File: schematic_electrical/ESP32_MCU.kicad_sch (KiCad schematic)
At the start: 14 parts, among them U1 ESP32_S2_PICO

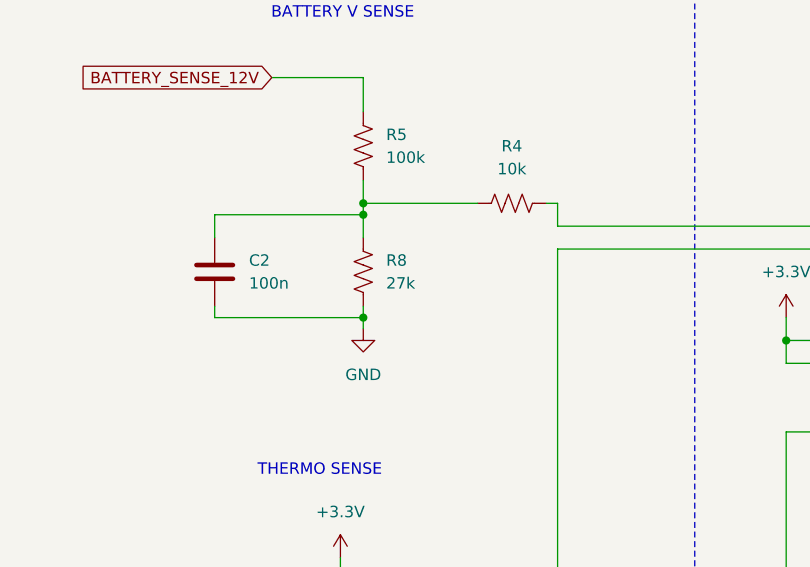
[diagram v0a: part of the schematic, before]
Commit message: Recalibrate thermistor, add reset reason to web UI, increase LED brightness
- Thermistor 2-point calibration redone with equilibrated reference points
  (48.3°F and 116°F); prior calibration used a non-equilibrated 156.9°F point
  that produced a bad slope. New: scale=0.9116, offset=+13.92°F
- Add last_reset_reason to telemetry API and web UI (esp_reset_reason())
- Increase PWM LED brightness from 33% to 66% duty cycle
- Schematic: update R8 value label to 22k (as built), clean CONNECTORS page

Co-Authored-By: Claude Sonnet 4.6 <noreply@anthropic.com>
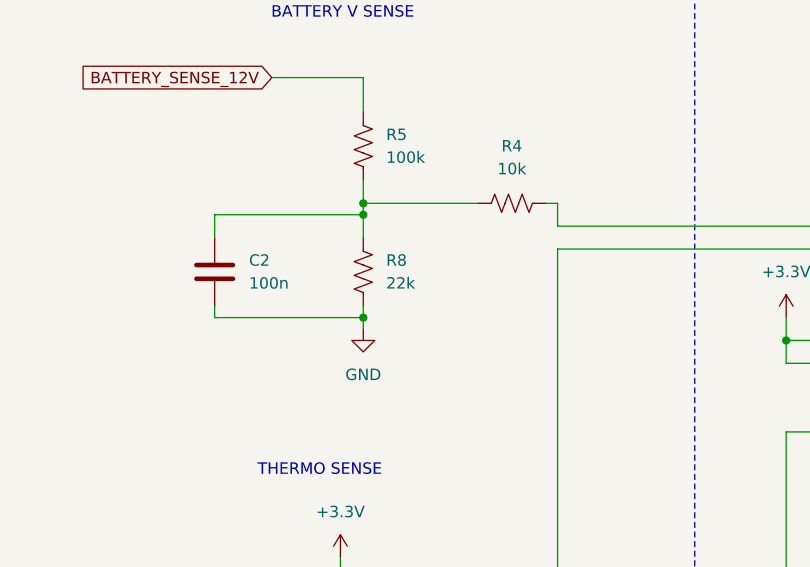
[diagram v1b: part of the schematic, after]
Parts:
- R8: value 27k -> 22k
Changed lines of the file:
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@@
 			)
 		)
-		(property "Value" "27k"
+		(property "Value" "22k"
 			(at 85.09 72.3899 0)
 			(effects

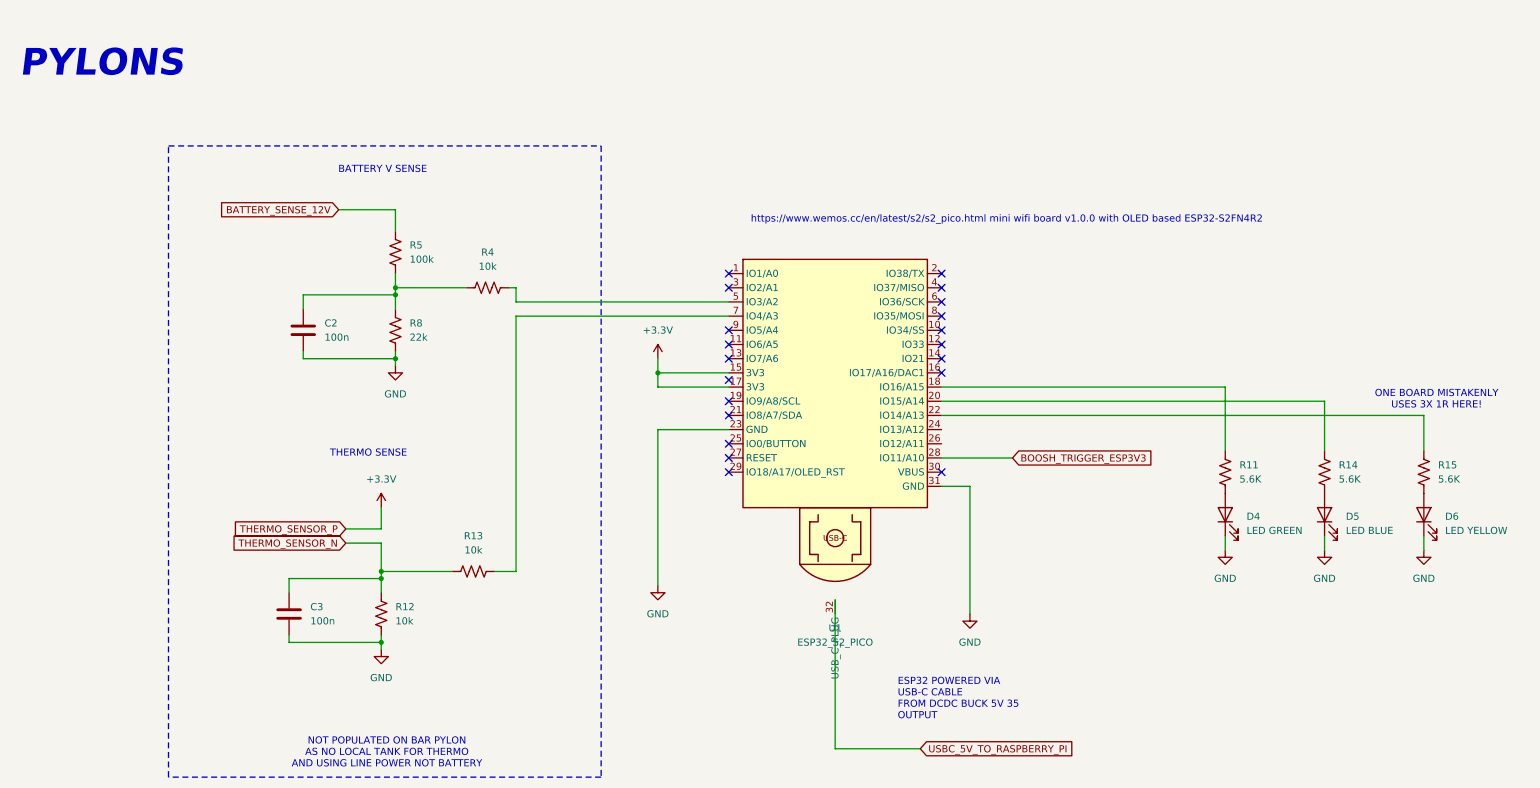
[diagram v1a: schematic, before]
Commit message: Add expansion buttons/lamps schematic sheet; schematic cleanup and annotations
- New EXPANSION_BUTTONS_LAMPS.kicad_sch sheet wired into top-level schematic
- Add AB_800T-QT24 symbol library
- ESP32_MCU: wire previously unconnected GPIO pins to BUTTON0-4 and BUTTON_LAMP_PWM_OUT0-4 global labels; add expansion IO bounding box annotation
- POWER: add GND ganging fabrication notes, DCDC USB wiring note, fuse value updated to "10A MINI AUTO BLADE"; routing cleanup
- CONNECTORS: routing and junction cleanup
- BOOSH_TRIGGER: remove stale "1R" errata note
- IDEA.md: add sandbox notes and open questions

Co-Authored-By: Claude Sonnet 4.6 <noreply@anthropic.com>
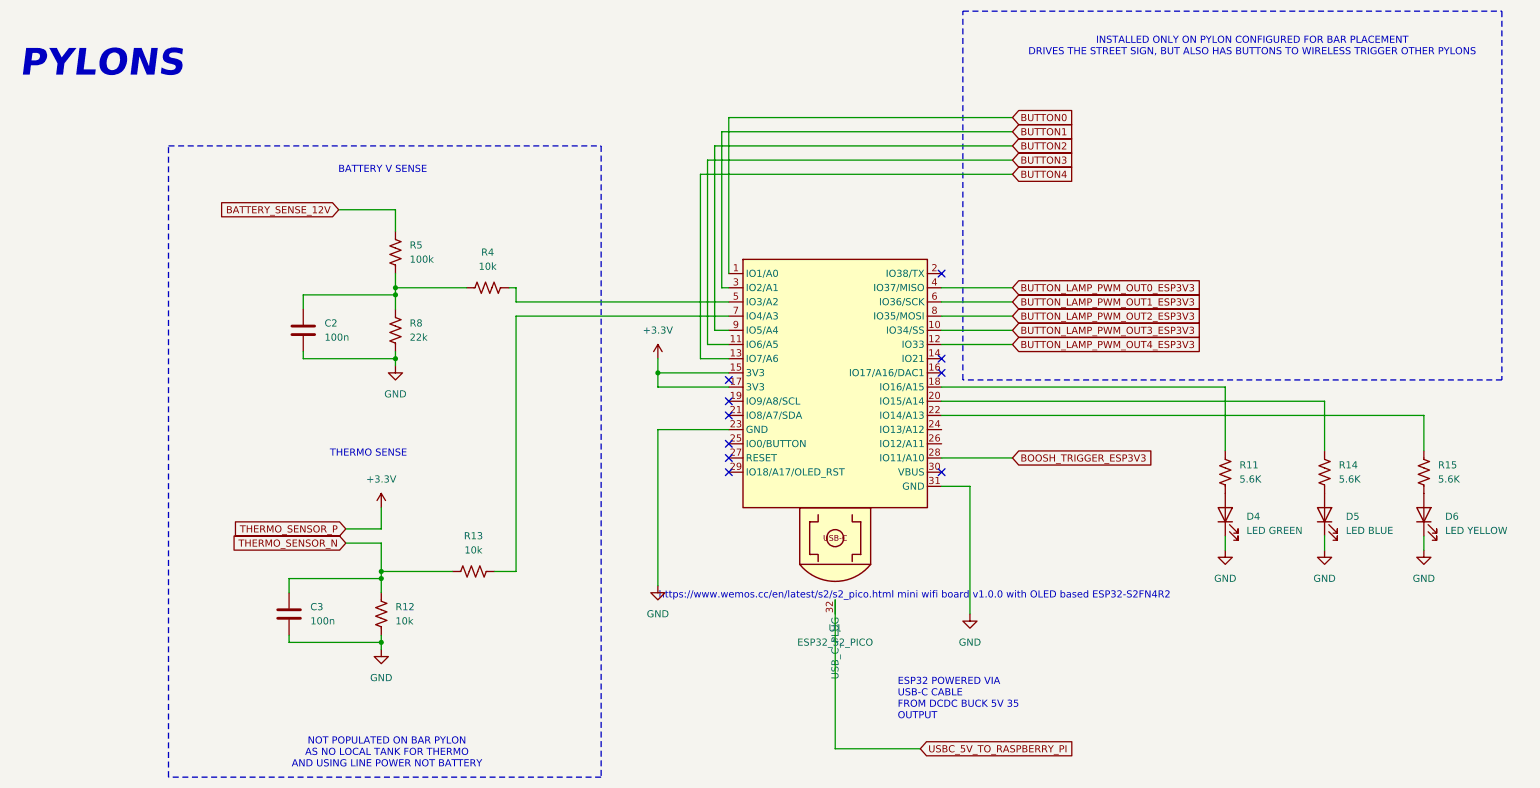
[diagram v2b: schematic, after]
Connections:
- net BUTTON0: now reaches U1.1 (IO1/A0)
- net BUTTON_LAMP_PWM_OUT3_ESP3V3: now reaches U1.10 (IO34/SS)
- net BUTTON3: now reaches U1.11 (IO6/A5)
- net BUTTON_LAMP_PWM_OUT4_ESP3V3: now reaches U1.12 (IO33)
- net BUTTON4: now reaches U1.13 (IO7/A6)
- net BUTTON1: now reaches U1.3 (IO2/A1)
- net BUTTON_LAMP_PWM_OUT0_ESP3V3: now reaches U1.4 (IO37/MISO)
- net BUTTON_LAMP_PWM_OUT1_ESP3V3: now reaches U1.6 (IO36/SCK)
- net BUTTON_LAMP_PWM_OUT2_ESP3V3: now reaches U1.8 (IO35/MOSI)
- net BUTTON2: now reaches U1.9 (IO5/A4)
- no-connect marks 20 -> 10
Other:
- note added: "INSTALLED ONLY ON PYLON CONFIGURED FOR BAR PLACEMENT DRIVES THE STREET SIGN, BUT ALSO HAS BUTTONS TO WIRELESS TRIGGER OTHER PYLONS"
- note removed: "ONE BOARD MISTAKENLY USES 3X 1R HERE!"
